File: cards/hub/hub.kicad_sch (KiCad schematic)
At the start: 34 parts, among them J1 BENCH +5V, J2 BENCH GND, J3 BUS, J4 BUS, Q1 BT151-500R

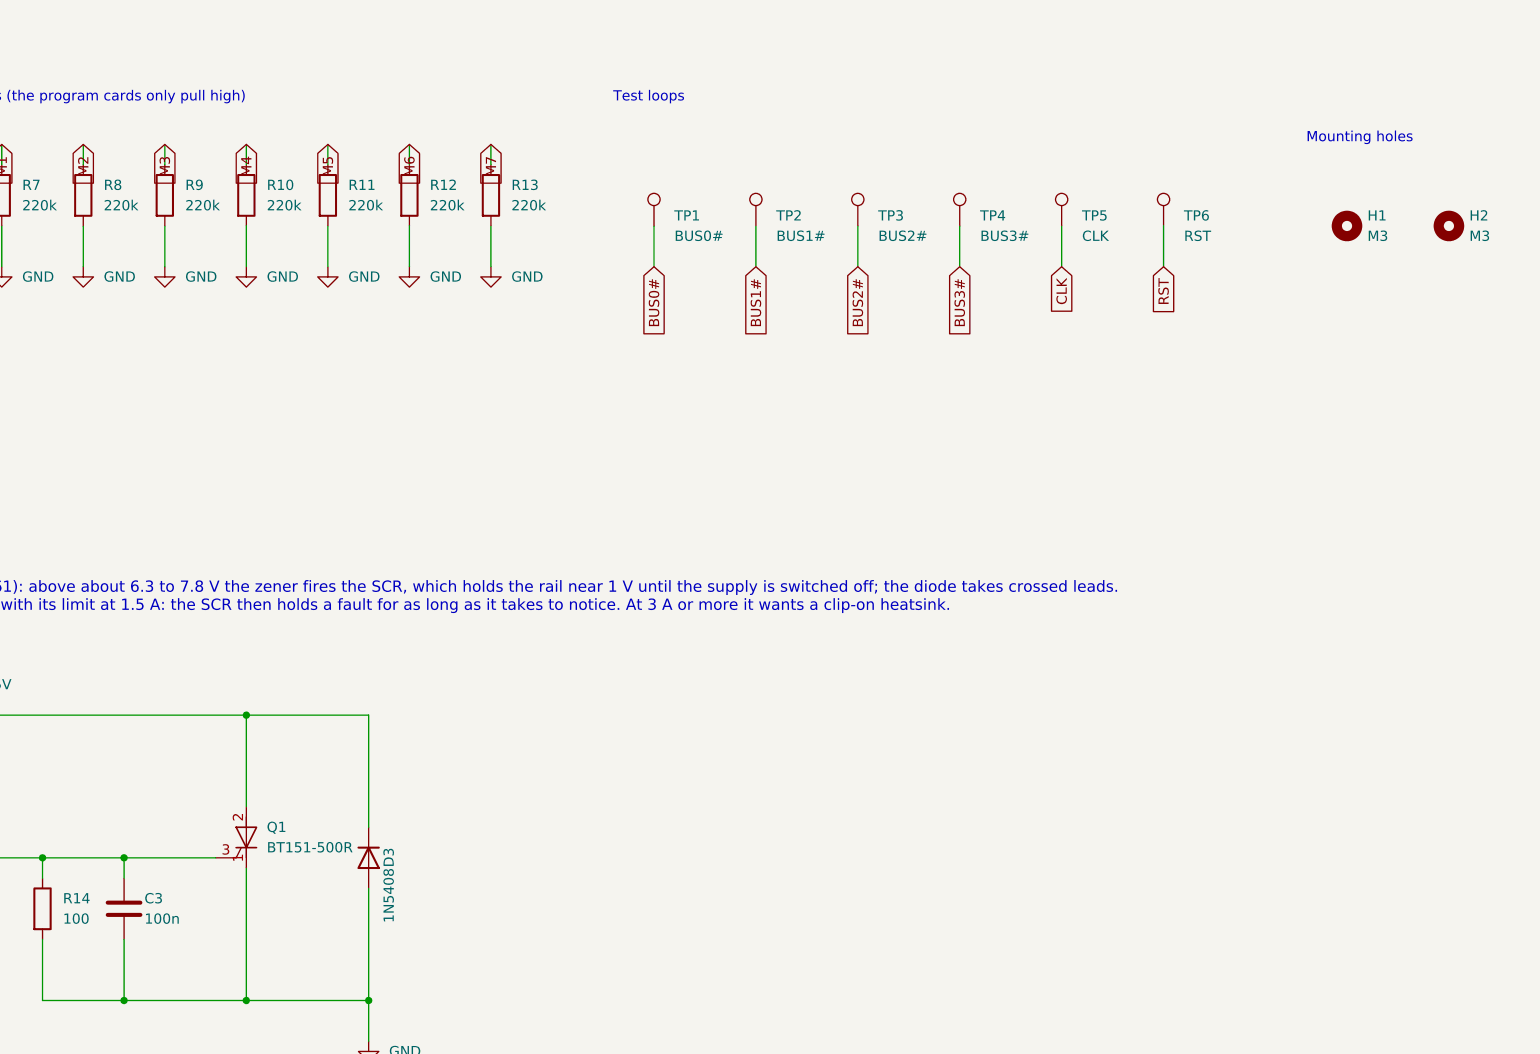
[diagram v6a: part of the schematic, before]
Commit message: Hub: an empty spot for the RST capacitor, so the fallback is a part and not leads on header pins
C-RST beside the RST test loop: pads for a 2.5 mm disc between RST and
ground, do-not-populate, in no parts list and not in the simulation (the
hub's export is the same, line for line, sorted). The simulation says the
pickup on RST stays at 0.3 to 0.4 V, under the 0.6 V it may
(rst_neighbour.md); if the scope says more, 2.2 nF goes here. Routed
again with freerouting 2.4.1, DRC clean, 0 unconnected, labels 1.0 mm.

Order gate: headers() reads a board's connectors in reference order; the
file's order shuffles on a rebuild and the self-test's planted fault on
the hub's second header went looking for a key that had moved.

bring-up.md section 9 and cards/README.md point at the spot.

Co-Authored-By: Claude Fable 5.1 <noreply@anthropic.com>
Claude-Session: https://claude.ai/code/session_01RktbhdQjDu7SpFpvkevyUU
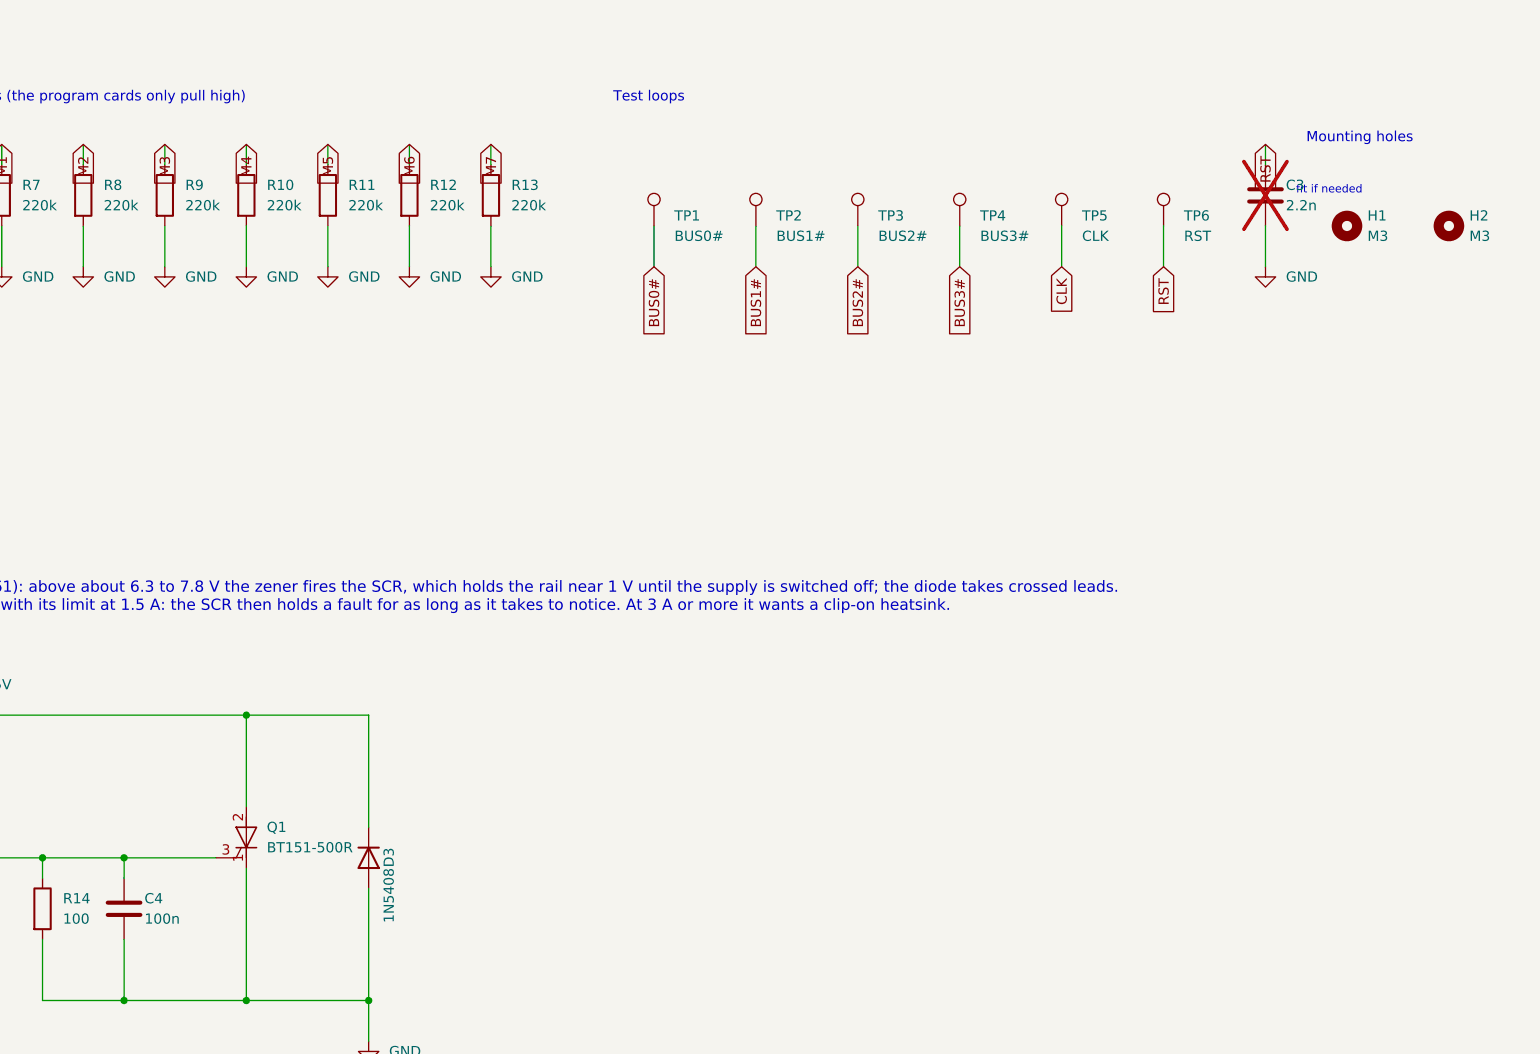
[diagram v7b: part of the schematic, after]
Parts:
- added C4: 100n, Capacitor_THT:C_Disc_D5.0mm_W2.5mm_P2.50mm, symbol Device:C
- C3: value 100n -> 2.2n; now not fitted; now left out of the parts list
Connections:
- net GND: now also C4.2
- net RST: now also C3.1
- net at D2.2 (A), Q1.3 (G), R14.1: now also C4.1; no longer C3.1
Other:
- note added: "fit if needed"
